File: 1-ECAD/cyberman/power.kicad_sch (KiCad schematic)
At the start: 51 parts, among them U10 DMN313DLT-7, U2 BQ25896RTWR, U3 S3B-ZR-SM4A-TF, U4 BQ27220YZFR, U5 RS3221-3.3YF3, U6 LM3281YFQR, U7 LM3281YFQR, U8 MMDT2907A-7-F, U9 DMP1045U-7

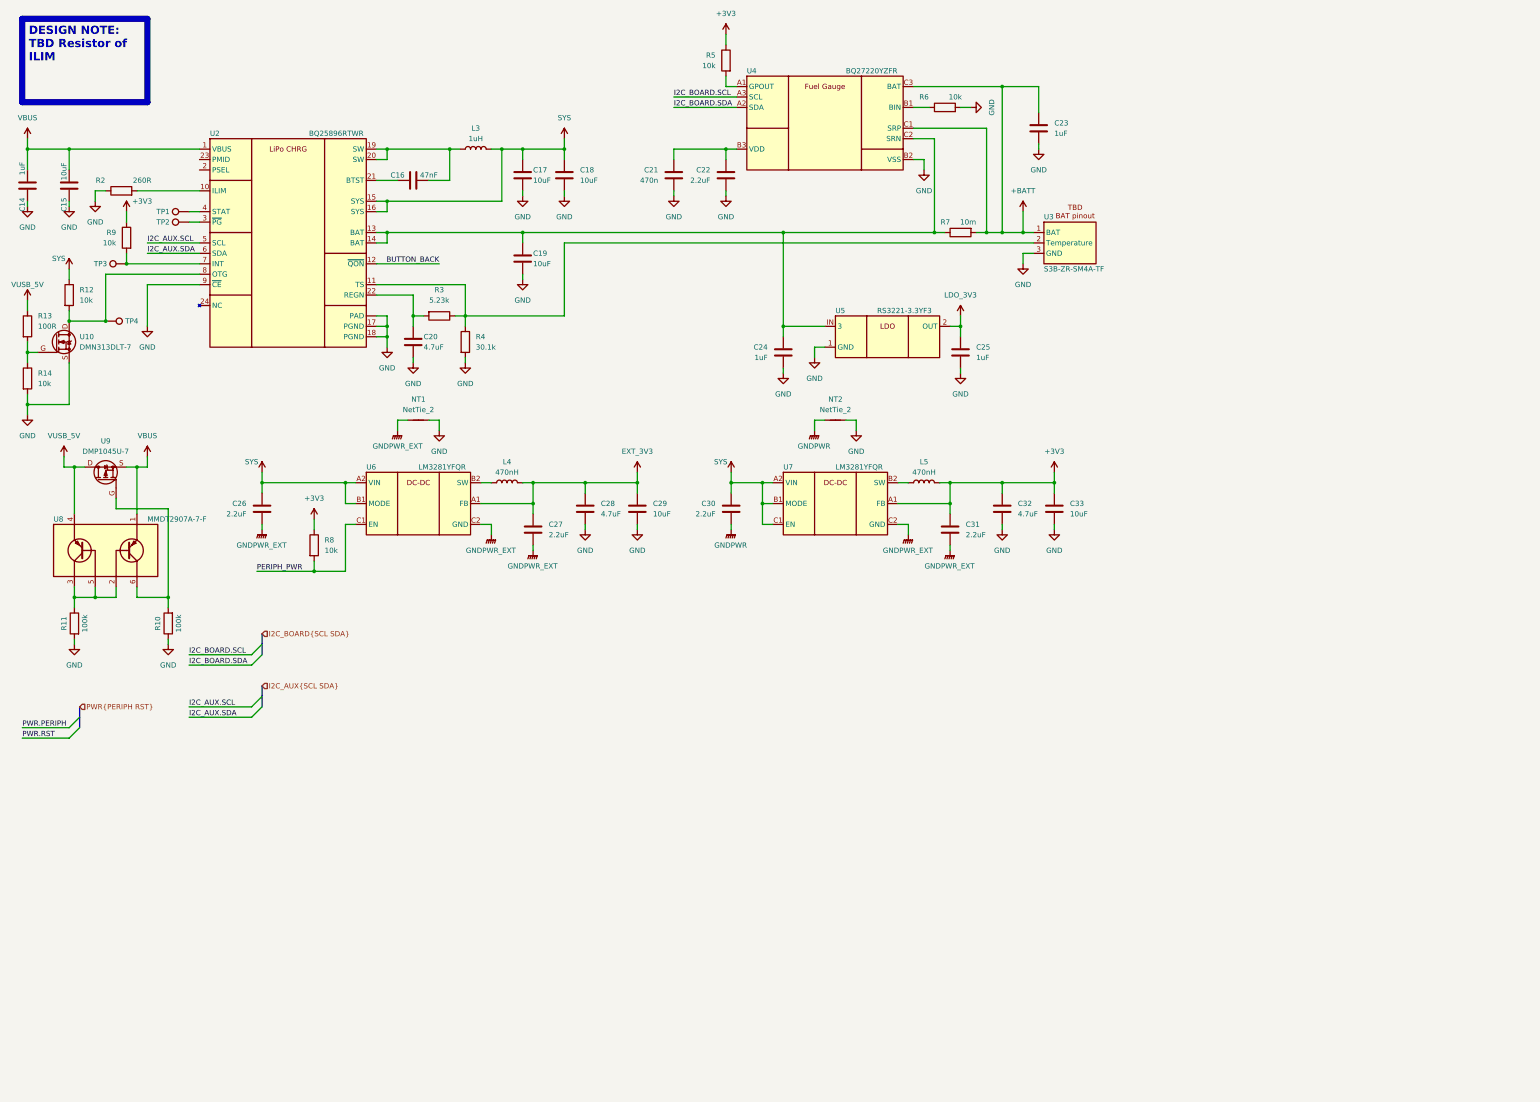
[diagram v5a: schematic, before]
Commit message: new changes
close display page and peripheral schematic
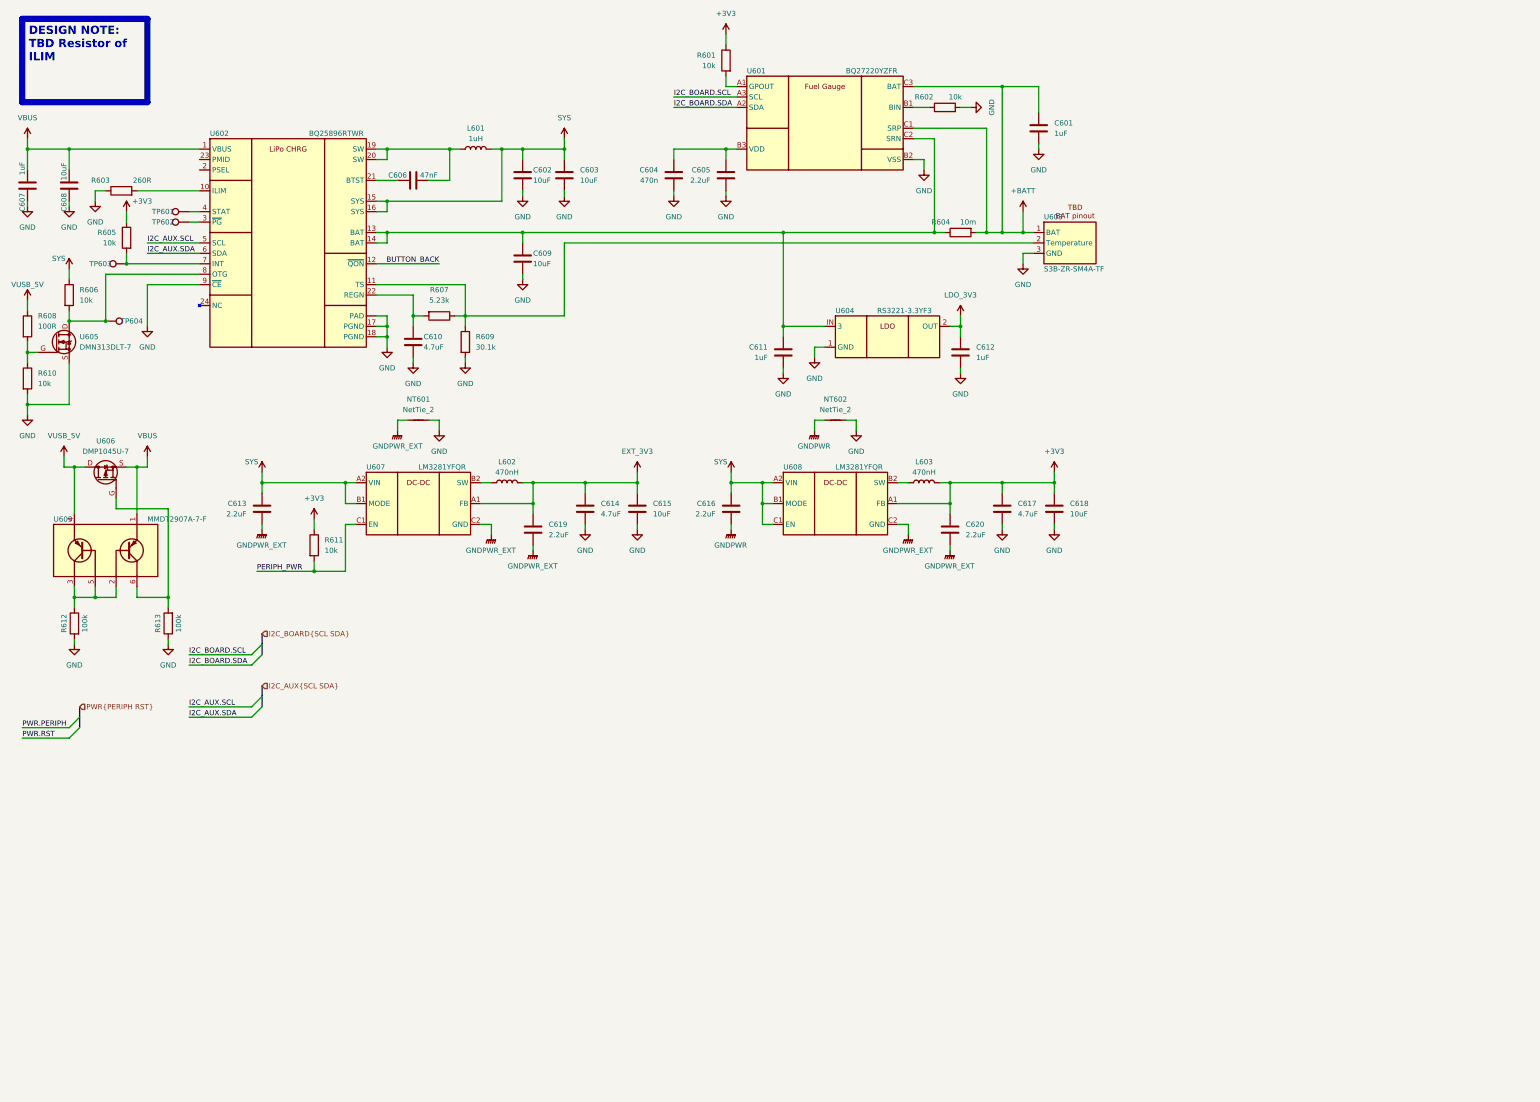
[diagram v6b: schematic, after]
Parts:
- renumbered C23 to C601, C17 to C602, C18 to C603, C21 to C604, C22 to C605, C16 to C606, C14 to C607, C15 to C608, C19 to C609, C20 to C610, C24 to C611, C25 to C612, C26 to C613, C28 to C614, C29 to C615, C30 to C616, C32 to C617, C33 to C618, C27 to C619, C31 to C620, L3 to L601, L4 to L602, L5 to L603, NT1 to NT601, NT2 to NT602, R5 to R601, R6 to R602, R2 to R603, R7 to R604, R9 to R605, R12 to R606, R3 to R607, R13 to R608, R4 to R609, R14 to R610, R8 to R611, R11 to R612, R10 to R613, TP1 to TP601, TP2 to TP602, TP3 to TP603, TP4 to TP604, U4 to U601, U2 to U602, U3 to U603, U5 to U604, U10 to U605, U9 to U606, U6 to U607, U7 to U608, U8 to U609
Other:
- company: (none) -> kode.

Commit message: change layout
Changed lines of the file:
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@@
+		)
+	)
+	(rectangle
+		(start 245.11 58.42)
+		(end 245.11 58.42)
+		(stroke
+			(width 0)
+			(type default)
+		)
+		(fill
+			(type none)
+		)
+	)
+	(rectangle
+		(start 189.23 17.78)
+		(end 238.76 63.5)
+		(stroke
+			(width 0)
+			(type default)
+		)
+		(fill
+			(type none)
+		)
+	)
+	(rectangle
+		(start 93.98 111.76)
+		(end 143.51 157.48)
+		(stroke
+			(width 0)
+			(type default)
+		)
+		(fill
+			(type none)
+		)
+	)
+	(rectangle
+		(start 193.04 109.22)
+		(end 242.57 154.94)
+		(stroke
+			(width 0)
+			(type default)
+		)
+		(fill
+			(type none)
 		)
 	)

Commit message: edit power page
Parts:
- removed C619, C620: 2.2uF, symbol Device:C
- removed NT601, NT602: NetTie_2, symbol Device:NetTie_2
- removed U601: BQ27220YZFR, 0_CI_smd:BQ27220YZFR, symbol 0_CI_smd:BQ27220YZFR
- removed U603: S3B-ZR-SM4A-TF, symbol 0_connector_smd:S3B-ZR-SM4A-TF
- removed U607, U608: LM3281YFQR, 0_converter_DCDC:LM3281YFQR, symbol 0_converterDCDC:LM3281YFQR
- added J601: S3B-ZR-SM4A-TF, 0_connector_smd:S3B-ZR-SM4A-TF, symbol 0_connector_smd:S3B-ZR-SM4A-TF
- added R614: 450k, symbol Device:R
- added R615: 100k, symbol Device:R
- added U601: MAX17048G+T10, 0_CI_smd:MAX17048G+T10, symbol 0_CI_smd:MAX17048G+T10
- added U607: TPS62825DMQR, 0_converter_DCDC:TPS6282x, symbol 0_converterDCDC:TPS62825DMQR
- added U608: TPS62824ADMQ, 0_converter_DCDC:TPS6282x, symbol 0_converterDCDC:TPS62824ADMQ
- C601: value 1uF -> 100n
- C604: value 470n -> 4.7uF
- C605: value 2.2uF -> 10uF
- C613, C616: value 2.2uF -> 120pF
- C614, C617: value 4.7uF -> 10uF
- C615: value 10uF -> 4.7uF
- R601, R611: value 10k -> 100k
- R602: value 10k -> 450k
- R604: value 10m -> 100k
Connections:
- net GNDPWR is gone; now on net GND: C616.2
- net GNDPWR_EXT is gone; now on net GND: C613.2
- net +3V3: now also C616.1, R614.1, U601.3 (VDD); no longer R601.1, R611.1
- net +BATT: now also C609.1, C611.1, U602.13 (BAT), U602.14 (BAT), U604.IN (3), J601.1 (BAT), U601.2 (CELL); no longer R604.2
- net EXT_3V3: now also C605.1, C613.1, R602.1; no longer C615.1
- net GND: now also R604.2, J601.3 (GND), R615.2, U601.1 (CTG), U601.4 (GND), U601.6 (QSTRT), U601.9 (EP), U607.4 (GND), U608.4 (GND); no longer R602.2
- net I2C_BOARD.SCL: now also U601.7 (SCL)
- net I2C_BOARD.SDA: now also U601.8 (SDA)
- net SYS: now also C604.1, C615.1, R601.1, R611.1, U607.6 (VIN), U608.1 (EN), U608.6 (VIN); no longer C613.1, C616.1
- net at R607.1, R609.1, U602.11 (TS): now also J601.2 (Temperature)
- net at L602.1: now also U607.5 (SW)
- net at L603.1: now also U608.5 (SW)
- net at R601.2: now also U607.2 (PG)
- net PERIPH_PWR: no longer names the net of R611.2
- net PERIPH_PWR: now also U608.2 (PG)
- new net: R602.2, R604.1, U607.3 (FB)
- new net: R614.2, R615.1, U608.3 (FB)
- new net FuelGauge_ALRT: U601.5 (~{ALRT})
- new net extENB: U607.1 (EN)
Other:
- note added: "Battery Connector"
- note added: "Battery and System Power Path Management"
- note added: "External 3V3 Power"
- note added: "Fuel Gauge"
- note added: "RTC LDO"
- note added: "System 3V3 Power"
- moved on the sheet: C602, C603, C606, C607, C608, C609, C610, C611, C612, L601, R603, R605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
